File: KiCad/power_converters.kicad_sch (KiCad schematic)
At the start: 22 parts, among them U4 TPS563231DRLR, U6 CSD25402Q3A

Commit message: Finished Rev 1 of the PCB
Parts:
- added D2: Green LED, LED_SMD:LED_0603_1608Metric_Pad1.05x0.95mm_HandSolder, symbol Device:LED
- added Q1: BSS138, Spiderbot:SOT-23_3L_ONS, symbol Simulation_SPICE:NMOS
- added R10: 2.1k, Resistor_SMD:R_0603_1608Metric_Pad0.98x0.95mm_HandSolder, symbol Device:R_US
- added R15: 10m, Resistor_SMD:R_1210_3225Metric_Pad1.30x2.65mm_HandSolder, symbol Device:R_US
- C1: renamed from C11; footprint (none) -> Capacitor_SMD:C_0603_1608Metric_Pad1.08x0.95mm_HandSolder
- C10: renamed from C9; value 100nF -> 0.1uF; footprint (none) -> Capacitor_SMD:C_0603_1608Metric_Pad1.08x0.95mm_HandSolder
- C2: renamed from C13; footprint (none) -> Spiderbot:PCAP_TPB_B2_PAN; Link (none) -> https://www.digikey.com/en/products/detail/panasonic-electr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
- C3: renamed from C6; footprint (none) -> Capacitor_SMD:C_0603_1608Metric_Pad1.08x0.95mm_HandSolder
- C4: renamed from C5; value 100nF -> 0.1uF; footprint (none) -> Capacitor_SMD:C_0603_1608Metric_Pad1.08x0.95mm_HandSolder
- C5: renamed from C12; footprint (none) -> Capacitor_SMD:C_0805_2012Metric_Pad1.18x1.45mm_HandSolder
- C6: renamed from C15; footprint (none) -> Capacitor_SMD:C_0805_2012Metric_Pad1.18x1.45mm_HandSolder
- C7: value 100nF -> 0.1uF; footprint (none) -> Capacitor_SMD:C_0603_1608Metric_Pad1.08x0.95mm_HandSolder
- C8: renamed from C10; footprint (none) -> Capacitor_SMD:C_0805_2012Metric_Pad1.18x1.45mm_HandSolder
- C9: renamed from C8; footprint (none) -> Capacitor_SMD:C_0603_1608Metric_Pad1.08x0.95mm_HandSolder
- D3: renamed from D2; footprint (none) -> Spiderbot:DIODE_SODB340_2P92X4P6_DIO; Link (none) -> https://www.digikey.com/en/products/detail/diodes-incorpora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
- L1: renamed from L2; footprint (none) -> Spiderbot:IND_SRP5030CA_BRN; Link (none) -> https://www.digikey.com/en/products/detail/bourns-inc/SRP50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
- L2: renamed from L1; footprint (none) -> Spiderbot:IND_BOURNS_SRN8040; Link (none) -> https://www.digikey.com/en/products/detail/bourns-inc/SRN80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
- R11: footprint (none) -> Resistor_SMD:R_0603_1608Metric_Pad0.98x0.95mm_HandSolder
- R12: renamed from R14; footprint (none) -> Resistor_SMD:R_0603_1608Metric_Pad0.98x0.95mm_HandSolder
- R13: renamed from R15; footprint (none) -> Resistor_SMD:R_0603_1608Metric_Pad0.98x0.95mm_HandSolder
- R14: renamed from R16; footprint (none) -> Resistor_SMD:R_0603_1608Metric_Pad0.98x0.95mm_HandSolder
- R16: renamed from R9; footprint (none) -> Resistor_SMD:R_0603_1608Metric_Pad0.98x0.95mm_HandSolder
- R51: renamed from R10; footprint (none) -> Resistor_SMD:R_0603_1608Metric_Pad0.98x0.95mm_HandSolder
- U1: renamed from 1; footprint MUA08A -> Spiderbot:MUA08A; Link (none) -> https://www.digikey.com/en/products/detail/texas-instrument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
- U2: renamed from U4; footprint DRL0006A -> Spiderbot:DRL0006A; Link (none) -> https://www.digikey.com/en/products/detail/texas-instrument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
- U3: renamed from U6; footprint CSD25402Q3A -> Spiderbot:CSD25402Q3A; Link (none) -> https://www.digikey.com/en/products/detail/texas-instrument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
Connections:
- net 6V_servo: now also Q1.2 (G), R10.1
- net 7.4V_batt: now also R15.1
- net GND: now also Q1.3 (S)
- net at U1.5 (ISEN), U3.1 (D): now also R15.2
- new net: D2.2 (A), R10.2
- new net: D2.1 (K), Q1.1 (D)
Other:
- moved on the sheet: C8

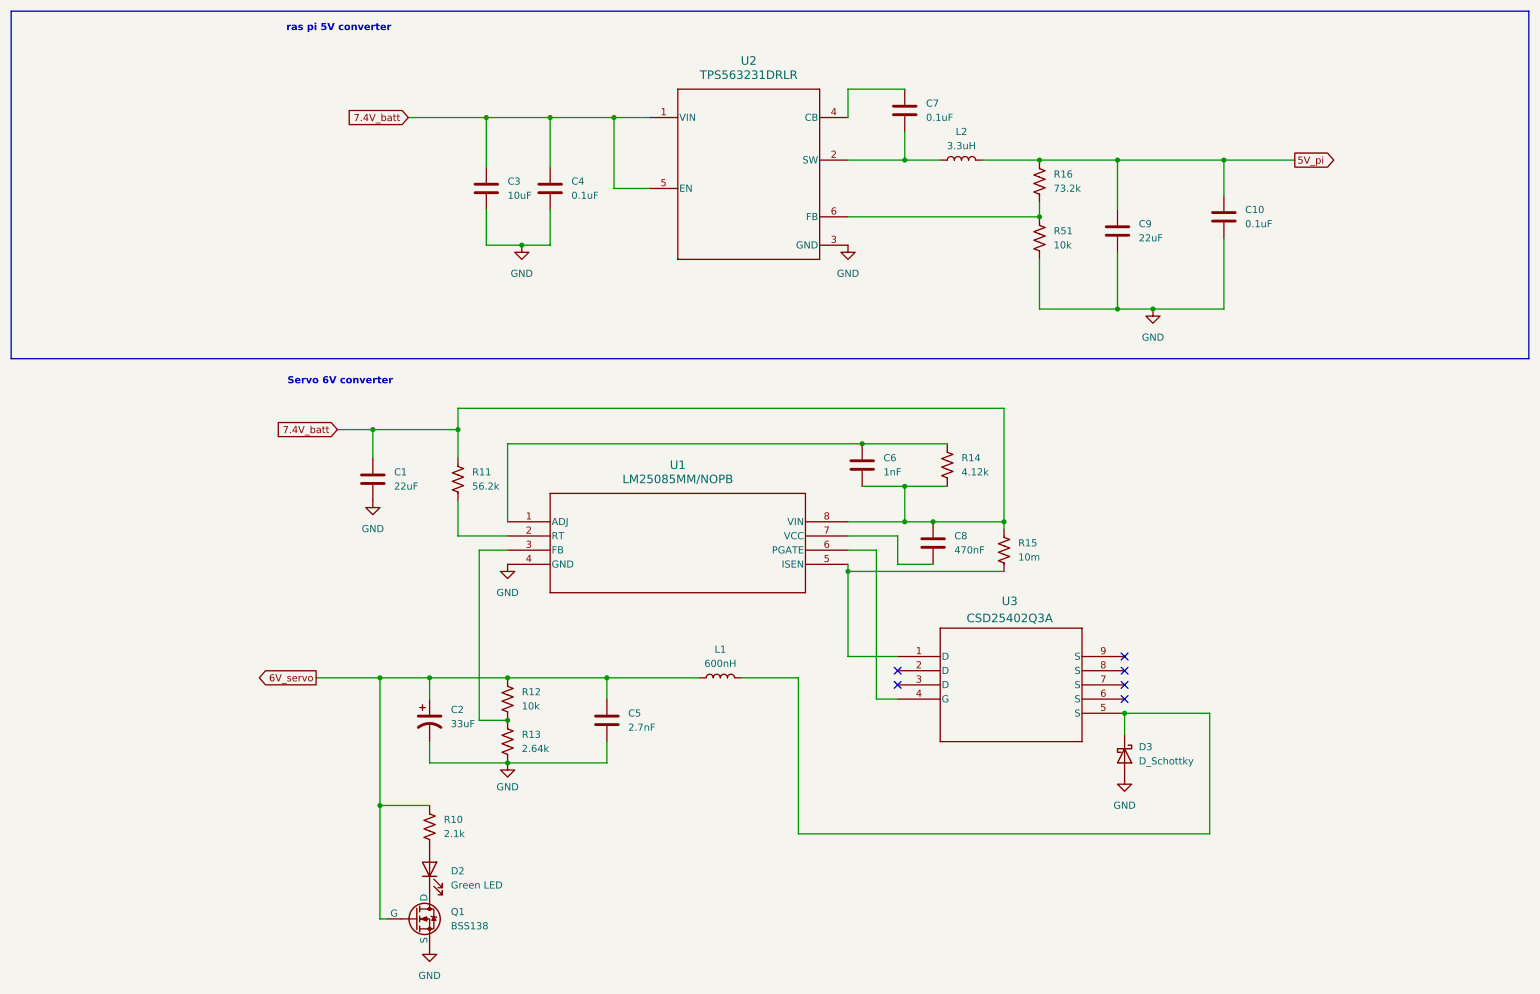
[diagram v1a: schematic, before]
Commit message: Changed 6V power line schematic
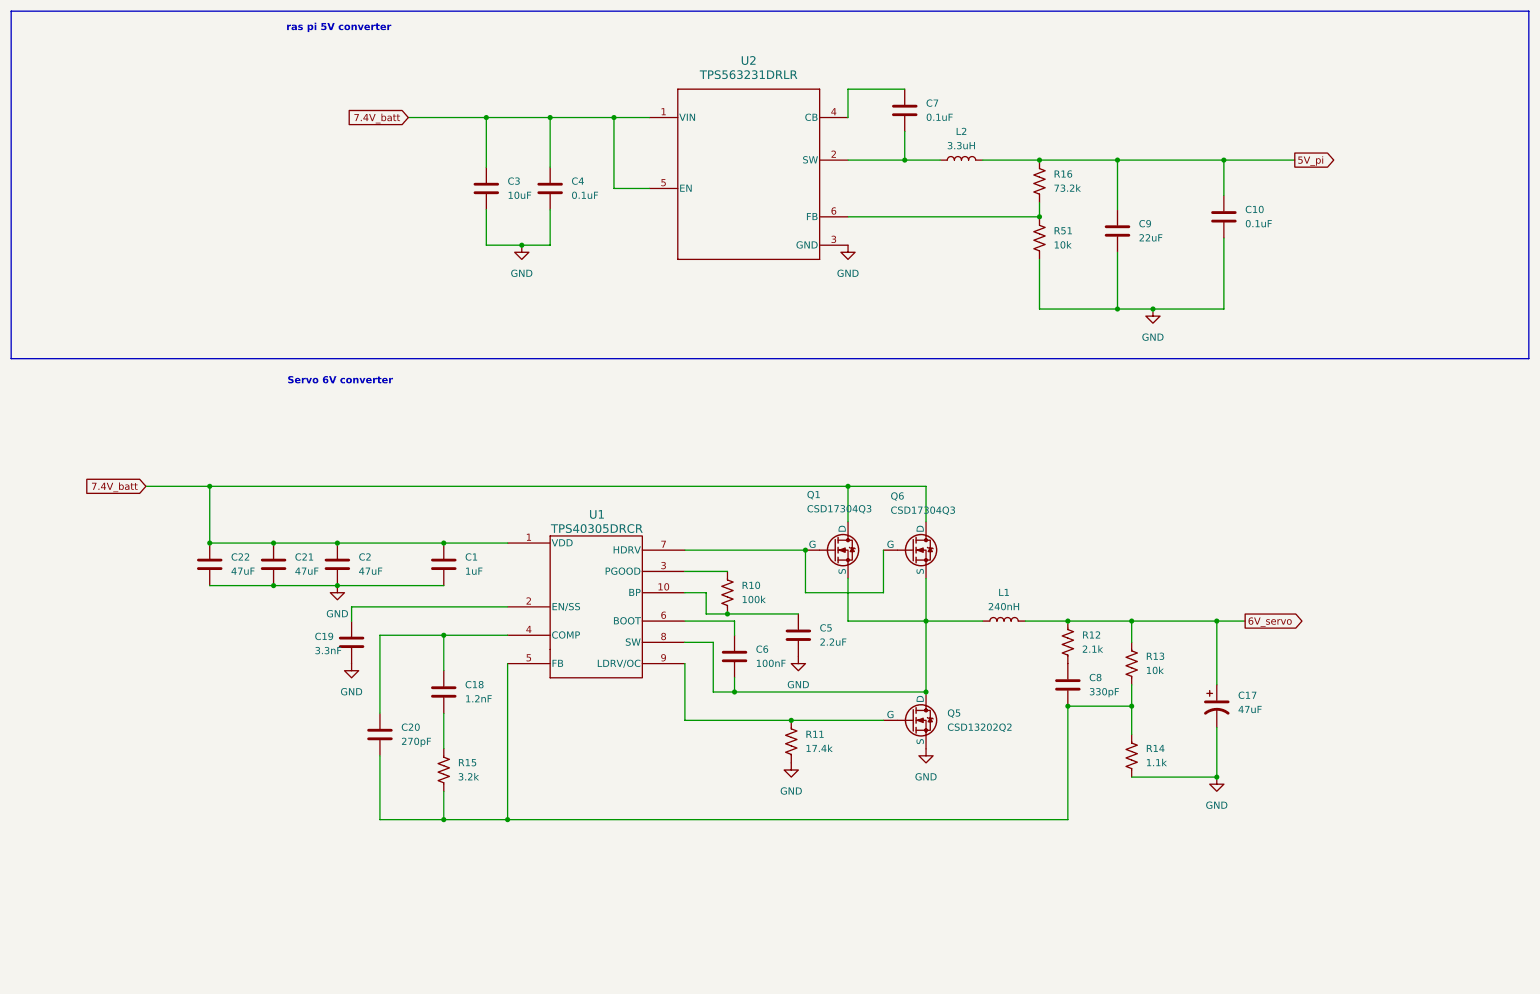
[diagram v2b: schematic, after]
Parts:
- removed C2: 33uF, Spiderbot:PCAP_TPB_B2_PAN, symbol Device:C_Polarized_US
- removed D2: Green LED, LED_SMD:LED_0603_1608Metric_Pad1.05x0.95mm_HandSolder, symbol Device:LED
- removed D3: D_Schottky, Spiderbot:DIODE_SODB340_2P92X4P6_DIO, symbol Device:D_Schottky
- removed U1: LM25085MM/NOPB, Spiderbot:MUA08A, symbol Alecs_Lib:LM25085MM_NOPB
- removed U3: CSD25402Q3A, Spiderbot:CSD25402Q3A, symbol Alecs_Lib:CSD25402Q3A
- added C17: 47uF, Spiderbot:PCAP_TPE_B2_PAN_1411, symbol Device:C_Polarized_US
- added C18: 1.2nF, symbol Device:C
- added C19: 3.3nF, symbol Device:C
- added C2, C21, C22: 47uF, symbol Device:C
- added C20: 270pF, symbol Device:C
- added Q5: CSD13202Q2, Spiderbot:Q2_SON6_TEX, symbol Simulation_SPICE:NMOS
- added Q6: CSD17304Q3, Spiderbot:Q2_SON6_TEX, symbol Simulation_SPICE:NMOS
- added U1: TPS40305DRCR, symbol Alecs_Lib:TPS40305DRCR
- C1: value 22uF -> 1uF; footprint Capacitor_SMD:C_0603_1608Metric_Pad1.08x0.95mm_HandSolder -> (none)
- C5: value 2.7nF -> 2.2uF; footprint Capacitor_SMD:C_0805_2012Metric_Pad1.18x1.45mm_HandSolder -> (none)
- C6: value 1nF -> 100nF; footprint Capacitor_SMD:C_0805_2012Metric_Pad1.18x1.45mm_HandSolder -> (none)
- C8: value 470nF -> 330pF; footprint Capacitor_SMD:C_0805_2012Metric_Pad1.18x1.45mm_HandSolder -> (none)
- L1: value 600nH -> 240nH; footprint Spiderbot:IND_SRP5030CA_BRN -> Spiderbot:IND_IHLP-4040DZ_VIS; Link https://www.digikey.com/en/products/detail/bourns-inc/SRP50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 -> (none)
- Q1: value BSS138 -> CSD17304Q3; footprint Spiderbot:SOT-23_3L_ONS -> Spiderbot:8VSON; Link https://www.digikey.com/en/products/detail/onsemi/BSS138/24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 -> (none)
- R10: value 2.1k -> 100k
- R11: value 56.2k -> 17.4k; footprint Resistor_SMD:R_0603_1608Metric_Pad0.98x0.95mm_HandSolder -> Resistor_SMD:R_0402_1005Metric_Pad0.72x0.64mm_HandSolder
- R12: value 10k -> 2.1k
- R13: value 2.64k -> 10k
- R14: value 4.12k -> 1.1k
- R15: value 10m -> 3.2k; footprint Resistor_SMD:R_1210_3225Metric_Pad1.30x2.65mm_HandSolder -> Capacitor_SMD:C_0805_2012Metric_Pad1.18x1.45mm_HandSolder
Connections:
- net 6V_servo: now also L1.2, R13.1, C17.1; no longer C5.1, L1.1, Q1.2 (G), R10.1
- net 7.4V_batt: now also Q1.1 (D), C2.1, C21.1, C22.1, Q6.1 (D), U1.1 (VDD); no longer C6.2, C8.1, R11.2, R14.2, R15.1
- net GND: now also R11.2, R14.2, C17.2, C19.2, C2.2, C21.2, C22.2, Q5.3 (S); no longer Q1.3 (S), R13.2
- net at R10.2: now also C5.1, U1.10 (BP)
- net at R12.2: now also C8.1; no longer R13.1
- net at R14.1: now also C8.2, R13.2, R15.2, C20.2, U1.5 (FB); no longer C6.1
- net at R11.1: now also Q5.2 (G), U1.9 (LDRV/OC)
- new net: Q1.2 (G), Q6.2 (G), U1.7 (HDRV)
- new net: C6.2, L1.1, Q1.3 (S), Q5.1 (D), Q6.3 (S), U1.8 (SW)
- new net: R10.1, U1.3 (PGOOD)
- new net: C18.1, C20.1, U1.4 (COMP)
- new net: C6.1, U1.6 (BOOT)
- new net: C18.2, R15.1
- new net: C19.1, U1.2 (EN/SS)
- no-connect marks 6 -> 0
